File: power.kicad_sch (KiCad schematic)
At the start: 29 parts, among them U21 TPS62A06DRLR, U22 INA228AQDGSRQ1, U23 INA187A2IDBVR

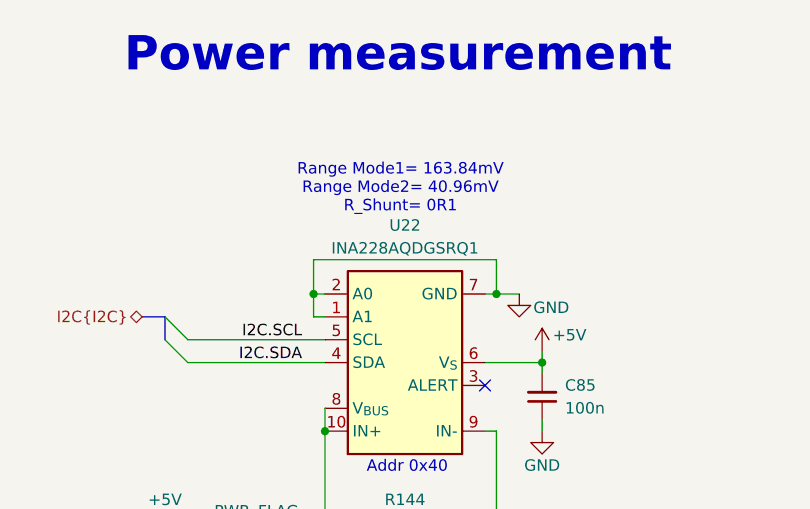
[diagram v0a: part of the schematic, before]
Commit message: [#95036] Solve ERC
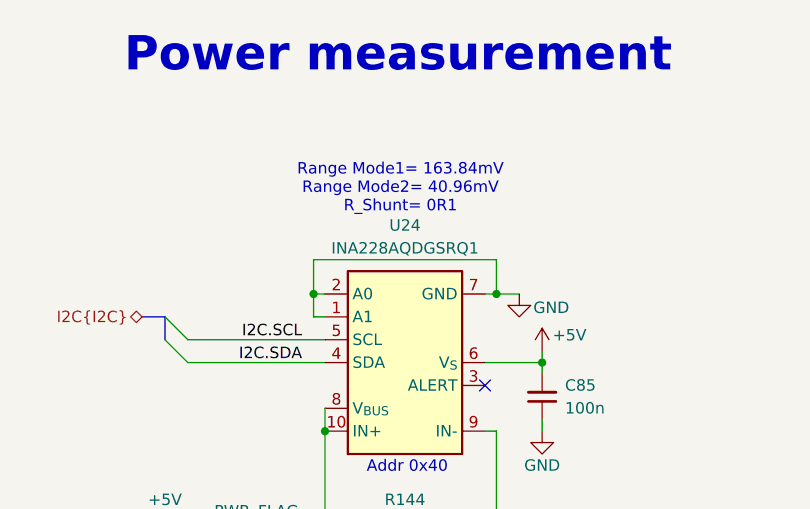
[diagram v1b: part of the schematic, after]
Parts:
- removed U22: INA228AQDGSRQ1, antmicro-footprints:VSSOP-10_3x3mm_P0.5mm, symbol antmicroPowerMeasurement:INA228AQDGSRQ1
- added U24: INA228AQDGSRQ1, antmicro-footprints:VSSOP-10_3x3mm_P0.5mm, symbol antmicroPowerMeasurement:INA228AQDGSRQ1
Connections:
- net +5V: now also U24.10 (IN+), U24.6 (V_{S}), U24.8 (V_{BUS})
- net +5V_Shunt: now also U24.9 (IN-)
- net GND: now also U24.1 (A1), U24.2 (A0), U24.7 (GND)
- net I2C.SCL: now also U24.5 (SCL)
- net I2C.SDA: now also U24.4 (SDA)
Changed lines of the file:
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@@
 	)
 	(junction
+		(at 173.99 96.52)
+		(diameter 0)
+		(color 0 0 0 0)
+	)
+	(junction
 		(at 245.11 177.8)
 		(diameter 0)
@@
 	)
 	(junction
-		(at 173.99 96.52)
-		(diameter 0)
-		(color 0 0 0 0)
-	)
-	(junction
 		(at 215.9 125.73)
 		(diameter 0)
@@
 	(wire
 		(pts
+			(xy 173.99 96.52) (xy 173.99 110.49)
+		)
+		(stroke
+			(width 0)
+			(type default)
+		)
+	)
+	(wire
+		(pts
 			(xy 172.72 77.47) (xy 193.04 77.47)
 		)
@@
 	(wire
 		(pts
-			(xy 173.99 96.52) (xy 173.99 110.49)
-		)
-		(stroke
-			(width 0)
-			(type default)
-		)
-	)
-	(wire
-		(pts
 			(xy 198.12 181.61) (xy 198.12 182.88)
 		)
@@
 	)
 	(symbol
-		(lib_id "antmicroPowerMeasurement:INA228AQDGSRQ1 ")
-		(at 173.99 96.52 0)
-		(mirror x)
-		(unit 1)
-		(exclude_from_sim no)
-		(in_bom yes)
-		(on_board yes)
-		(dnp no)
-		(fields_autoplaced yes)
-		(property "Reference" "U22"
-			(at 182.88 73.66 0)
-			(effects
-				(font
-					(size 1.27 1.27)
-					(thickness 0.15)
-				)
-			)
-		)
-		(property "Value" "INA228AQDGSRQ1"
-			(at 204.47 88.9 0)
-			(effects
-				(font
-					(size 1.27 1.27)
-					(thickness 0.15)
-				)
-				(justify left bottom)
-				(hide yes)
-			)
-		)
-		(property "Footprint" "antmicro-footprints:VSSOP-10_3x3mm_P0.5mm"
-			(at 204.47 86.36 0)
-			(effects
-				(font
-					(size 1.27 1.27)
-					(thickness 0.15)
-				)
-				(justify left bottom)
-				(hide yes)
-			)
-		)
-		(property "Datasheet" "https://www.ti.com/lit/gpn/ina228-q1"
-			(at 204.47 83.82 0)
-			(effects
-				(font
-					(size 1.27 1.27)
-					(thickness 0.15)
-				)
-				(justify left bottom)
-				(hide yes)
-			)
-		)
-		(property "Description" "85V, 20-bit, ultra-precise power/energy/charge monitor with IC interface"
-			(at 204.47 73.66 0)
-			(effects
-				(font
-					(size 1.27 1.27)
-				)
-				(justify left bottom)
-				(hide yes)
-			)
-		)
-		(property "Manufacturer" "Texas Instruments"
-			(at 204.47 81.28 0)
-			(effects
-				(font
-					(size 1.27 1.27)
-					(thickness 0.15)
-				)
-				(justify left bottom)
-				(hide yes)
-			)
-		)
-		(property "MPN" "INA228AQDGSRQ1 "
-			(at 182.88 76.2 0)
-			(effects
-				(font
-					(size 1.27 1.27)
-					(thickness 0.15)
-				)
-			)
-		)
-		(property "Author" "Antmicro"
-			(at 204.47 78.74 0)
-			(effects
-				(font
-					(size 1.27 1.27)
-					(thickness 0.15)
-				)
-				(justify left bottom)
-				(hide yes)
-			)
-		)
-		(property "License" "Apache-2.0"
-			(at 204.47 76.2 0)
-			(effects
-				(font
-					(size 1.27 1.27)
-					(thickness 0.15)
-				)
-				(justify left bottom)
-				(hide yes)
-			)
-		)
-		(pin "3"
-		)
-		(pin "10"
-		)
-		(pin "1"
-		)
-		(pin "7"
-		)
-		(pin "2"
-		)
-		(pin "9"
-		)
-		(pin "6"
-		)
-		(pin "8"
-		)
-		(pin "4"
-		)
-		(pin "5"
-		)
-		(instances
-			(project "renode-reference-platform"
-				(path "/126ae87b-f292-4372-94ff-ae46971d67ab/3bbe31bb-f2b9-4019-b1b8-20b6749deb1b"
-					(reference "U22")
-					(unit 1)
-				)
-			)
-		)
-	)
-	(symbol
 		(lib_id "antmicroCapacitors0402:C_10u_0402")
 		(at 129.54 185.42 90)
@@
 					(unit 1)
 				)
+			)
+		)
+	)
+	(symbol
+		(lib_id "antmicroPowerMeasurement:INA228AQDGSRQ1")
+		(at 173.99 96.52 0)
+		(mirror x)
+		(unit 1)
+		(exclude_from_sim no)
+		(in_bom yes)
+		(on_board yes)
+		(dnp no)
+		(fields_autoplaced yes)
+		(property "Reference" "U24"
+			(at 182.88 73.66 0)
+			(effects
+				(font
+					(size 1.27 1.27)
+					(thickness 0.15)
+				)
+			)
+		)
+		(property "Value" "INA228AQDGSRQ1"
+			(at 204.47 88.9 0)
+			(effects
+				(font
+					(size 1.27 1.27)
+					(thickness 0.15)
+				)
+				(justify left bottom)
+				(hide yes)
+			)
+		)
+		(property "Footprint" "antmicro-footprints:VSSOP-10_3x3mm_P0.5mm"
+			(at 204.47 86.36 0)
+			(effects
+				(font
+					(size 1.27 1.27)
+					(thickness 0.15)
+				)
+				(justify left bottom)
+				(hide yes)
+			)
+		)
+		(property "Datasheet" "https://www.ti.com/lit/gpn/ina228-q1"
+			(at 204.47 83.82 0)
+			(effects
+				(font
+					(size 1.27 1.27)
+					(thickness 0.15)
+				)
+				(justify left bottom)
+				(hide yes)
+			)
+		)
+		(property "Description" "85V, 20-bit, ultra-precise power/energy/charge monitor with IC interface"
+			(at 204.47 73.66 0)
+			(effects
+				(font
+					(size 1.27 1.27)
+				)
+				(justify left bottom)
+				(hide yes)
+			)
+		)
+		(property "Manufacturer" "Texas Instruments"
+			(at 204.47 81.28 0)
+			(effects
+				(font
+					(size 1.27 1.27)
+					(thickness 0.15)
+				)
+				(justify left bottom)
+				(hide yes)
+			)
+		)
+		(property "MPN" "INA228AQDGSRQ1"
+			(at 182.88 76.2 0)
+			(effects
+				(font
+					(size 1.27 1.27)
+					(thickness 0.15)
+				)
+			)
+		)
+		(property "Author" "Antmicro"
+			(at 204.47 78.74 0)
+			(effects
+				(font
+					(size 1.27 1.27)
+					(thickness 0.15)
+				)
+				(justify left bottom)
+				(hide yes)
+			)
+		)
+		(property "License" "Apache-2.0"
+			(at 204.47 76.2 0)
+			(effects
+				(font
+					(size 1.27 1.27)
+					(thickness 0.15)
+				)
+				(justify left bottom)
+				(hide yes)
+			)
+		)
+		(pin "6"
+		)
+		(pin "7"
+		)
+		(pin "9"
+		)
+		(pin "3"
+		)
+		(pin "10"
+		)
+		(pin "5"
+		)
+		(pin "4"
+		)
+		(pin "8"
+		)
+		(pin "1"
+		)
+		(pin "2"
+		)
+		(instances
+			(project "renode-reference-platform"
+				(path "/126ae87b-f292-4372-94ff-ae46971d67ab/3bbe31bb-f2b9-4019-b1b8-20b6749deb1b"
+					(reference "U24")
+					(unit 1)
+				)

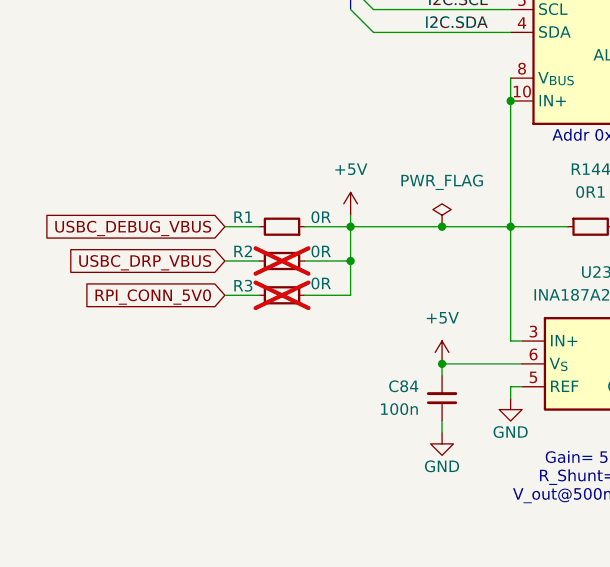
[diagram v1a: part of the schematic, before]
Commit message: [#95398] Initial component placement
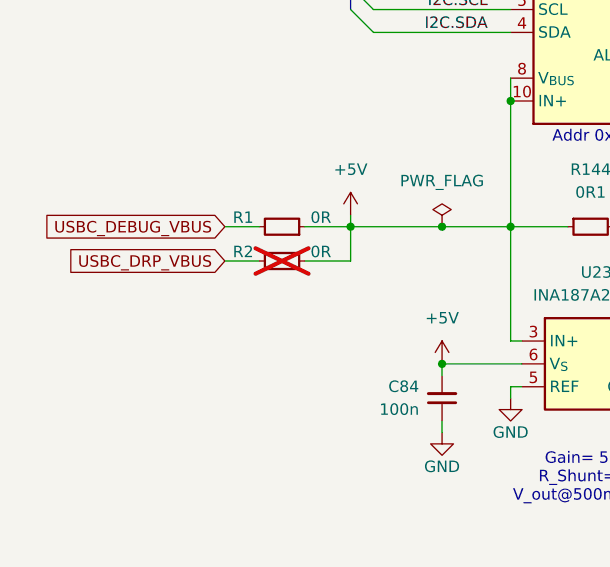
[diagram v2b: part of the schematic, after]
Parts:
- removed R3: R_0R_0402, antmicro-footprints:R_0402_1005Metric, symbol antmicroResistors0402:R_0R_0402
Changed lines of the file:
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@@
 	)
 	(junction
-		(at 156.21 114.3)
-		(diameter 0)
-		(color 0 0 0 0)
-	)
-	(junction
 		(at 205.74 125.73)
 		(diameter 0)
@@
 	(wire
 		(pts
-			(xy 151.13 118.11) (xy 156.21 118.11)
-		)
-		(stroke
-			(width 0)
-			(type default)
-		)
-	)
-	(wire
-		(pts
 			(xy 172.72 83.82) (xy 173.99 83.82)
 		)
@@
 	(wire
 		(pts
-			(xy 142.24 118.11) (xy 146.05 118.11)
-		)
-		(stroke
-			(width 0)
-			(type default)
-		)
-	)
-	(wire
-		(pts
 			(xy 138.43 185.42) (xy 138.43 186.69)
 		)
@@
 	(wire
 		(pts
-			(xy 156.21 118.11) (xy 156.21 114.3)
-		)
-		(stroke
-			(width 0)
-			(type default)
-		)
-	)
-	(wire
-		(pts
 			(xy 158.75 86.36) (xy 173.99 86.36)
 		)
@@
 		)
 	)
-	(global_label "RPI_CONN_5V0"
-		(shape input)
-		(at 142.24 118.11 180)
-		(fields_autoplaced yes)
-		(effects
-			(font
-				(size 1.27 1.27)
-				(thickness 0.1588)
-			)
-			(justify right)
-		)
-		(property "Intersheetrefs" "${INTERSHEET_REFS}"
-			(at 125.4057 118.11 0)
-			(effects
-				(font
-					(size 1.27 1.27)
-				)
-				(justify right)
-			)
-		)
-	)
 	(global_label "USBC_DRP_VBUS"
 		(shape input)
@@
 					(unit 1)
 				)
-			)
-		)
-	)
-	(symbol
-		(lib_id "antmicroResistors0402:R_0R_0402")
-		(at 151.13 118.11 180)
-		(unit 1)
-		(exclude_from_sim no)
-		(in_bom yes)
-		(on_board yes)
-		(dnp yes)
-		(property "Reference" "R3"
-			(at 144.272 117.094 0)
-			(effects
-				(font
-					(size 1.27 1.27)
-					(thickness 0.15)
-				)
-			)
-		)
-		(property "Value" "R_0R_0402"
-			(at 130.81 105.41 0)
-			(effects
-				(font
-					(size 1.27 1.27)
-					(thickness 0.15)
-				)
-				(justify left bottom)
-				(hide yes)
-			)
-		)
-		(property "Footprint" "antmicro-footprints:R_0402_1005Metric"
-			(at 130.81 102.87 0)
-			(effects
-				(font
-					(size 1.27 1.27)
-					(thickness 0.15)
-				)
-				(justify left bottom)
-				(hide yes)
-			)
-		)
-		(property "Datasheet" "https://industrial.panasonic.com/cdbs/www-data/pdf/RDA0000/AOA0000C301.pdf"
-			(at 130.81 100.33 0)
-			(effects
-				(font
-					(size 1.27 1.27)
-					(thickness 0.15)
-				)
-				(justify left bottom)
-				(hide yes)
-			)
-		)
-		(property "Description" "SMD Chip Resistor, Jumper, 0 ohm, 100 mW, 0402 [1005 Metric], Thick Film, General Purpose"
-			(at 130.81 85.09 0)
-			(effects
-				(font
-					(size 1.27 1.27)
-				)
-				(justify left bottom)
-				(hide yes)
-			)
-		)
-		(property "MPN" "ERJ2GE0R00X"
-			(at 130.81 97.79 0)
-			(effects
-				(font
-					(size 1.27 1.27)
-					(thickness 0.15)
-				)
-				(justify left bottom)
-				(hide yes)
-			)
-		)
-		(property "Manufacturer" "Panasonic"
-			(at 130.81 95.25 0)
-			(effects
-				(font
-					(size 1.27 1.27)
-					(thickness 0.15)
-				)
-				(justify left bottom)
-				(hide yes)
-			)
-		)
-		(property "License" "Apache-2.0"
-			(at 130.81 92.71 0)
-			(effects
-				(font
-					(size 1.27 1.27)
-					(thickness 0.15)
-				)
-				(justify left bottom)
-				(hide yes)
-			)
-		)
-		(property "Author" "Antmicro"
-			(at 130.81 90.17 0)
-			(effects
-				(font
-					(size 1.27 1.27)
-					(thickness 0.15)
-				)
-				(justify left bottom)
-				(hide yes)
-			)
-		)
-		(property "Val" "0R"
-			(at 152.908 116.84 0)
-			(effects
-				(font
-					(size 1.27 1.27)
-					(thickness 0.15)
-				)
-			)
-		)
-		(property "Tolerance" "~"
-			(at 130.81 107.95 0)
-			(effects
-				(font
-					(size 1.27 1.27)
-				)
-				(justify left bottom)
-				(hide yes)
-			)
-		)
-		(property "Current" "1A"
-			(at 130.81 87.63 0)
-			(effects
-				(font
-					(size 1.27 1.27)
-					(thickness 0.15)
-				)
-				(justify left bottom)
-				(hide yes)
-			)
-		)
-		(pin "2"
-		)
-		(pin "1"
-		)
-		(instances
-			(project "renode-reference-platform"
-				(path "/126ae87b-f292-4372-94ff-ae46971d67ab/3bbe31bb-f2b9-4019-b1b8-20b6749deb1b"
-					(reference "R3")
-					(unit 1)
-				)

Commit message: [#95398] Schematic cleanup
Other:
- moved on the sheet: C81, C82, C83, C84, C85, C86, C87, C88, C89, C90, C91, D17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

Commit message: [#95398] Add markings for ETH strap resistors
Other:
- title: renode-reference-platform -> STM32H7 Renode Reference Platform
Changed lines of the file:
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@@
 	(paper "A3")
 	(title_block
-		(title "renode-reference-platform")
+		(title "STM32H7 Renode Reference Platform")
 		(date "07.04.2026")
 		(rev "1.0.0")
